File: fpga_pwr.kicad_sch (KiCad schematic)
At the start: 32 parts, among them U3H LFE5U-25F-8MG285C, U3I LFE5U-25F-8MG285C

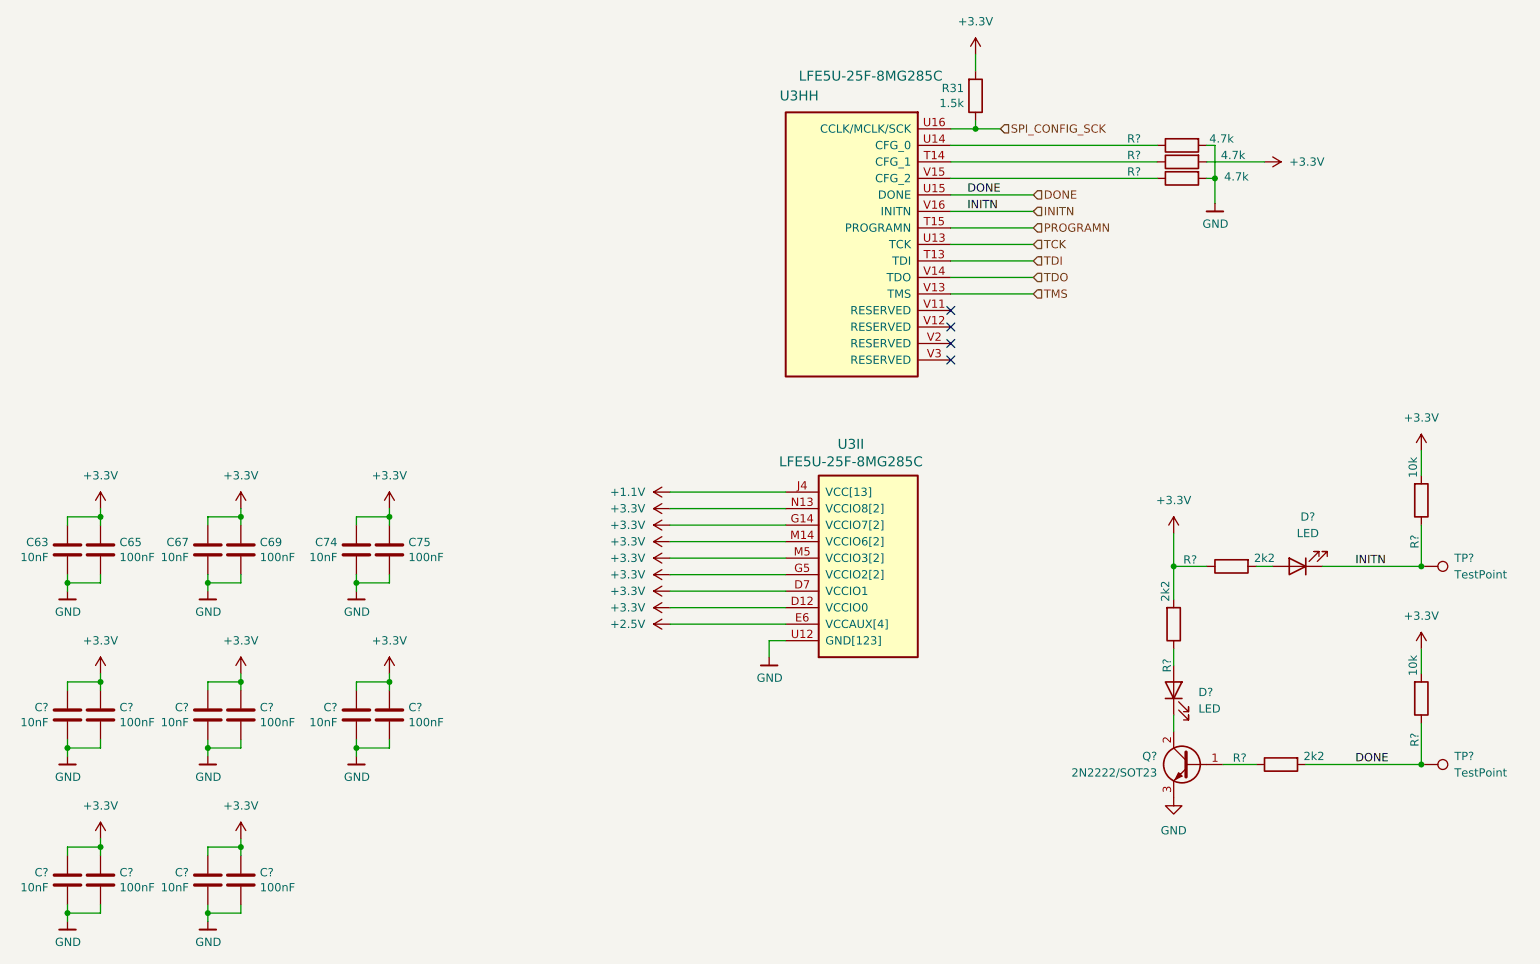
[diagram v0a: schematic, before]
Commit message: start to assign footprint
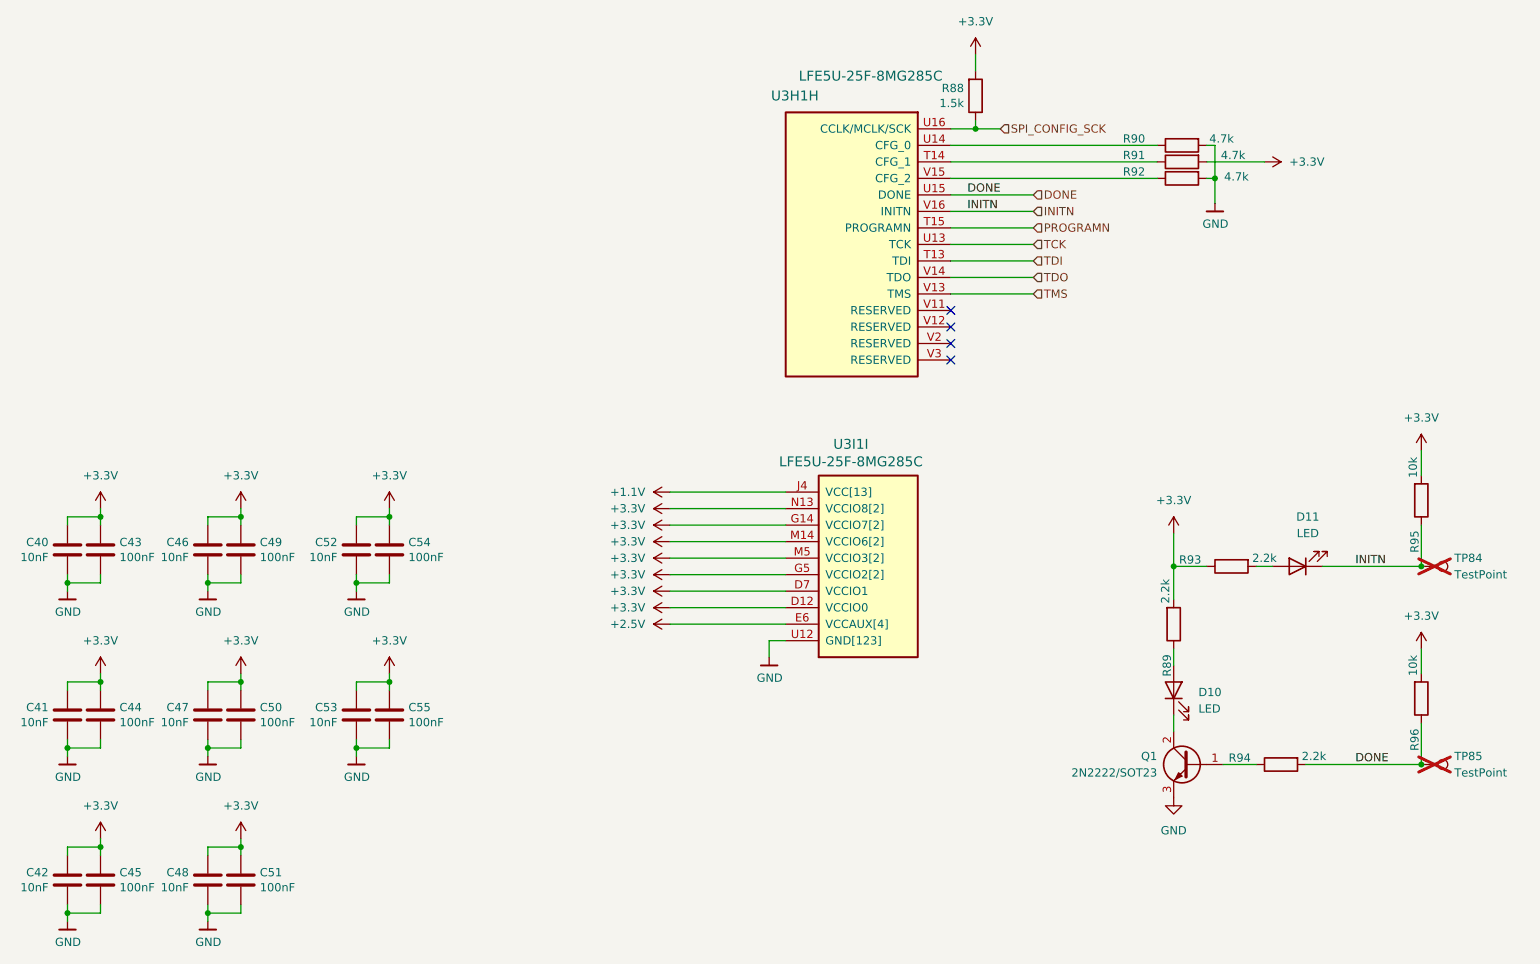
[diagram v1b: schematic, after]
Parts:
- C40: renamed from C63; footprint gkl_dipol:C_0201_0603Metric -> Capacitor_SMD:C_0603_1608Metric
- C41, C42, C44, C45, C47, C48, C50, C51, C53, C55: renamed from C?; footprint gkl_dipol:C_0201_0603Metric -> Capacitor_SMD:C_0603_1608Metric
- C43: renamed from C65; footprint gkl_dipol:C_0201_0603Metric -> Capacitor_SMD:C_0603_1608Metric
- C46: renamed from C67; footprint gkl_dipol:C_0201_0603Metric -> Capacitor_SMD:C_0603_1608Metric
- C49: renamed from C69; footprint gkl_dipol:C_0201_0603Metric -> Capacitor_SMD:C_0603_1608Metric
- C52: renamed from C74; footprint gkl_dipol:C_0201_0603Metric -> Capacitor_SMD:C_0603_1608Metric
- C54: renamed from C75; footprint gkl_dipol:C_0201_0603Metric -> Capacitor_SMD:C_0603_1608Metric
- D10, D11: renamed from D?; footprint (none) -> Diode_SMD:D_0603_1608Metric
- Q1: renamed from Q?; footprint (none) -> Package_TO_SOT_SMD:SOT-23-3
- R88: renamed from R31; footprint gkl_dipol:R_0201_0603Metric -> Resistor_SMD:R_0603_1608Metric
- R89, R93, R94: renamed from R?; value 2k2 -> 2.2k; footprint gkl_dipol:R_0201_0603Metric -> Resistor_SMD:R_0603_1608Metric
- R90, R91, R92, R95, R96: renamed from R?; footprint gkl_dipol:R_0201_0603Metric -> Resistor_SMD:R_0603_1608Metric
- TP84, TP85: renamed from TP?; footprint (none) -> TestPoint:TestPoint_THTPad_D1.5mm_Drill0.7mm; now not fitted
- renumbered U3H to U3H1, U3I to U3I1

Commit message: Assign jlcpcb pn. Fix footprint assign, uniform resistor value for battery charger
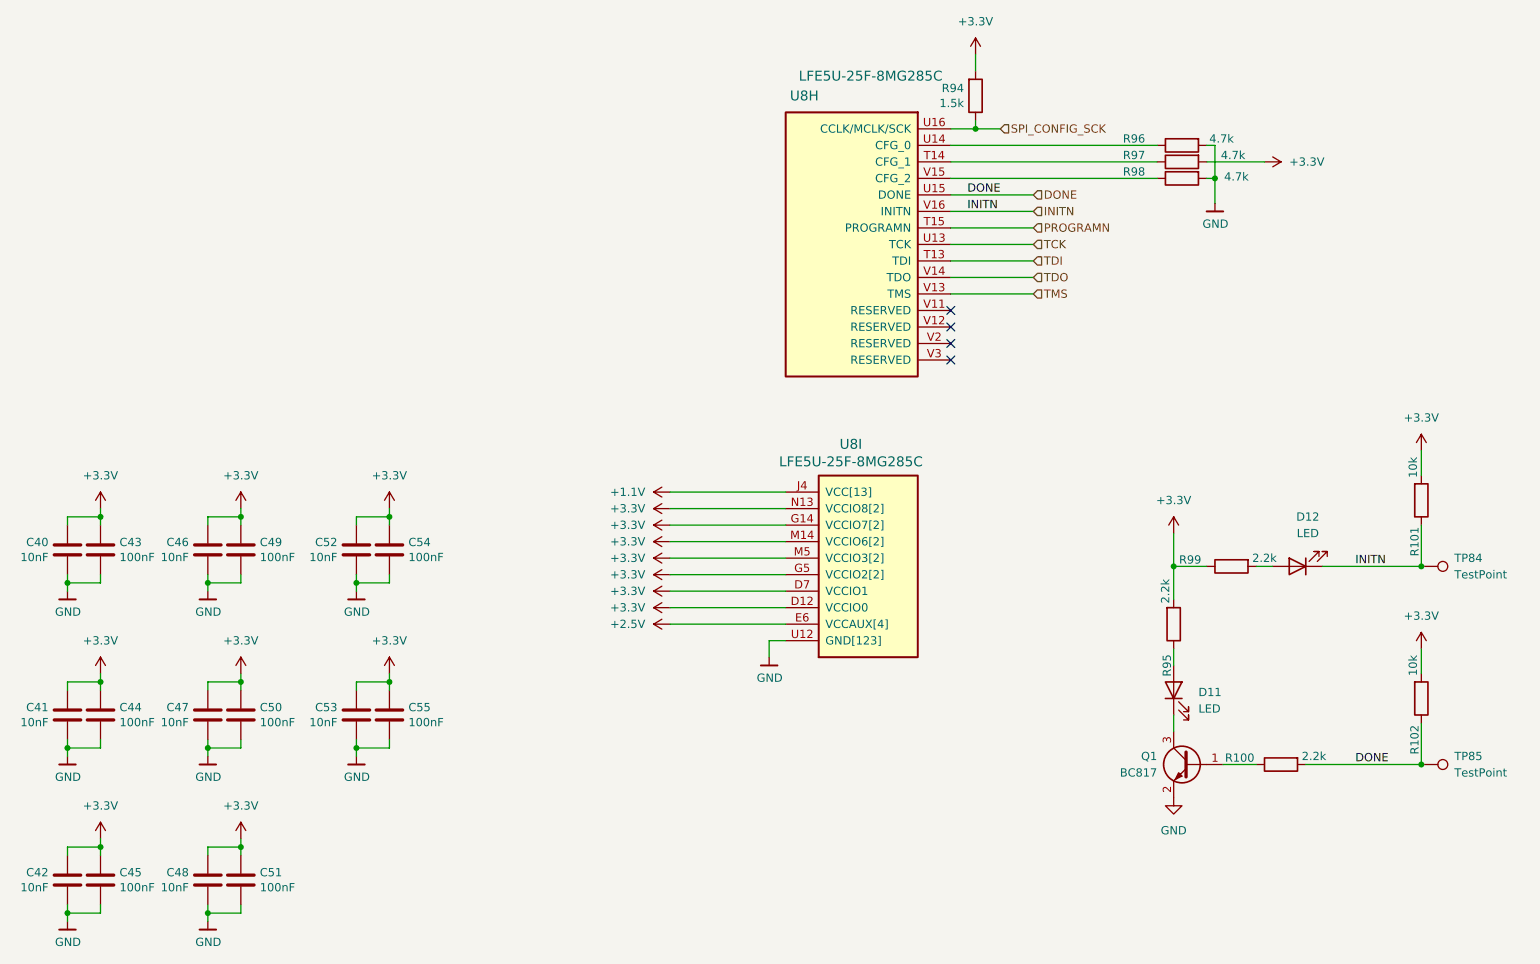
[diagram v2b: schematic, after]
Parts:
- removed Q1: 2N2222/SOT23, Package_TO_SOT_SMD:SOT-23-3, symbol Transistor_BJT:Q_NPN_BCE
- added Q1: BC817, Package_TO_SOT_SMD:SOT-23, symbol Transistor_BJT:BC817
- TP84, TP85: now fitted; now left out of the parts list
- U8: renamed from U3H1; footprint gkl_housings_bga:csBGA285 -> kicad:BGA-285
- U8: renamed from U3I1; footprint gkl_housings_bga:csBGA285 -> kicad:BGA-285
- renumbered D10 to D11, D11 to D12, R94 to R100, R95 to R101, R96 to R102, R88 to R94, R89 to R95, R90 to R96, R91 to R97, R92 to R98, R93 to R99
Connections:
- net GND: now also Q1.2 (E)
- net at R100.1: now also Q1.1 (B)
- net at D11.1 (K): now also Q1.3 (C)

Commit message: routing sram
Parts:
- R100: LCSC (none) -> C4190
- R94: LCSC (none) -> C22843
- U8: ComponentClass (none) -> fanout; LCSC (none) -> C5664013
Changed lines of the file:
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@@
 			)
 		)
+		(property "ComponentClass" "fanout"
+			(at 181.61 52.07 0)
+			(effects
+				(font
+					(size 1.27 1.27)
+				)
+				(hide yes)
+			)
+		)
+		(property "LCSC" "C5664013"
+			(at 181.61 52.07 0)
+			(effects
+				(font
+					(size 1.27 1.27)
+				)
+				(hide yes)
+			)
+		)
 		(pin "E6"
 		)
@@
 			)
 		)
+		(property "ComponentClass" "fanout"
+			(at 156.21 130.81 0)
+			(effects
+				(font
+					(size 1.27 1.27)
+				)
+				(hide yes)
+			)
+		)
+		(property "LCSC" "C5664013"
+			(at 156.21 130.81 0)
+			(effects
+				(font
+					(size 1.27 1.27)
+				)
+				(hide yes)
+			)
+		)
 		(pin "B11"
 		)
@@
 			)
 		)
+		(property "LCSC" "C4190"
+			(at 232.41 149.86 0)
+			(effects
+				(font
+					(size 1.27 1.27)
+				)
+				(hide yes)
+			)
+		)
 		(pin "1"
 		)
@@
 			(at 185.42 46.99 0)
 			(effects
+				(font
+					(size 1.27 1.27)
+				)
+				(hide yes)
+			)
+		)
+		(property "LCSC" "C22843"
+			(at 185.42 46.99 0)
+			(effects

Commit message: Continue routing
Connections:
- net +1.1V: now also C42.1, C45.1
- net +2.5V: now also C48.1, C51.1
- net +3.3V: no longer C42.1, C45.1, C48.1, C51.1
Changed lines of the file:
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@@
 			)
 		)
-		(property "Value" "+3.3V"
+		(property "Value" "+1.1V"
 			(at 50.8 156.21 0)
 			(effects
@@
 			)
 		)
-		(property "Value" "+3.3V"
+		(property "Value" "+2.5V"
 			(at 72.39 156.21 0)
 			(effects

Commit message: continue routing
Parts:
- removed TP84, TP85: TestPoint, TestPoint:TestPoint_THTPad_D1.5mm_Drill0.7mm, symbol Connector:TestPoint
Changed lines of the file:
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@@
 	)
 	(junction
-		(at 254 149.86)
-		(diameter 0)
-		(color 0 0 0 0)
-	)
-	(junction
 		(at 50.8 137.16)
 		(diameter 0)
@@
 	)
 	(junction
-		(at 254 119.38)
-		(diameter 0)
-		(color 0 0 0 0)
-	)
-	(junction
 		(at 95.25 137.16)
 		(diameter 0)
@@
 	)
 	(symbol
-		(lib_id "Connector:TestPoint")
-		(at 254 119.38 270)
-		(unit 1)
-		(exclude_from_sim no)
-		(in_bom no)
-		(on_board yes)
-		(dnp no)
-		(fields_autoplaced yes)
-		(property "Reference" "TP84"
-			(at 259.08 118.1099 90)
-			(effects
-				(font
-					(size 1.27 1.27)
-				)
-				(justify left)
-			)
-		)
-		(property "Value" "TestPoint"
-			(at 259.08 120.6499 90)
-			(effects
-				(font
-					(size 1.27 1.27)
-				)
-				(justify left)
-			)
-		)
-		(property "Footprint" "TestPoint:TestPoint_THTPad_D1.5mm_Drill0.7mm"
-			(at 254 124.46 0)
-			(effects
-				(font
-					(size 1.27 1.27)
-				)
-				(hide yes)
-			)
-		)
-		(property "Datasheet" "~"
-			(at 254 124.46 0)
-			(effects
-				(font
-					(size 1.27 1.27)
-				)
-				(hide yes)
-			)
-		)
-		(property "Description" "test point"
-			(at 254 119.38 0)
-			(effects
-				(font
-					(size 1.27 1.27)
-				)
-				(hide yes)
-			)
-		)
-		(property "KLC_S3.3" ""
-			(at 254 119.38 90)
-			(effects
-				(font
-					(size 1.27 1.27)
-				)
-				(hide yes)
-			)
-		)
-		(property "KLC_S4.1" ""
-			(at 254 119.38 90)
-			(effects
-				(font
-					(size 1.27 1.27)
-				)
-				(hide yes)
-			)
-		)
-		(pin "1"
-		)
-		(instances
-			(project ""
-				(path "/d6c42660-1080-4fbd-a2d9-2a0cd6b4e770/12e9a14f-df84-4ea1-a186-cc5705defdaf"
-					(reference "TP84")
-					(unit 1)
-				)
-			)
-		)
-	)
-	(symbol
 		(lib_id "power:+3.3V")
 		(at 138.43 128.27 90)
@@
 					(unit 1)
 				)
-			)
-		)
-	)
-	(symbol
-		(lib_id "Connector:TestPoint")
-		(at 254 149.86 270)
-		(unit 1)
-		(exclude_from_sim no)
-		(in_bom no)
-		(on_board yes)
-		(dnp no)
-		(fields_autoplaced yes)
-		(property "Reference" "TP85"
-			(at 259.08 148.5899 90)
-			(effects
-				(font
-					(size 1.27 1.27)
-				)
-				(justify left)
-			)
-		)
-		(property "Value" "TestPoint"
-			(at 259.08 151.1299 90)
-			(effects
-				(font
-					(size 1.27 1.27)
-				)
-				(justify left)
-			)
-		)
-		(property "Footprint" "TestPoint:TestPoint_THTPad_D1.5mm_Drill0.7mm"
-			(at 254 154.94 0)
-			(effects
-				(font
-					(size 1.27 1.27)
-				)
-				(hide yes)
-			)
-		)
-		(property "Datasheet" "~"
-			(at 254 154.94 0)
-			(effects
-				(font
-					(size 1.27 1.27)
-				)
-				(hide yes)
-			)
-		)
-		(property "Description" "test point"
-			(at 254 149.86 0)
-			(effects
-				(font
-					(size 1.27 1.27)
-				)
-				(hide yes)
-			)
-		)
-		(property "KLC_S3.3" ""
-			(at 254 149.86 90)
-			(effects
-				(font
-					(size 1.27 1.27)
-				)
-				(hide yes)
-			)
-		)
-		(property "KLC_S4.1" ""
-			(at 254 149.86 90)
-			(effects
-				(font
-					(size 1.27 1.27)
-				)
-				(hide yes)
-			)
-		)
-		(pin "1"
-		)
-		(instances
-			(project "fpgaler"
-				(path "/d6c42660-1080-4fbd-a2d9-2a0cd6b4e770/12e9a14f-df84-4ea1-a186-cc5705defdaf"
-					(reference "TP85")
-					(unit 1)
-				)
